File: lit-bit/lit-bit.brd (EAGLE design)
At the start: 37.5 x 49.5 mm, 71 parts, among them J2 USB_MICRO_B_SMD_FEMALE, J3 ISP, U2 32U4, U3 73831, U4 ADXL345, U5 S-1335, U6 MCP7940N, U7 24FC1025, Y1 8MHz, Y2 32.768kHz, Y3 32.768kHz, Y4 16MHz

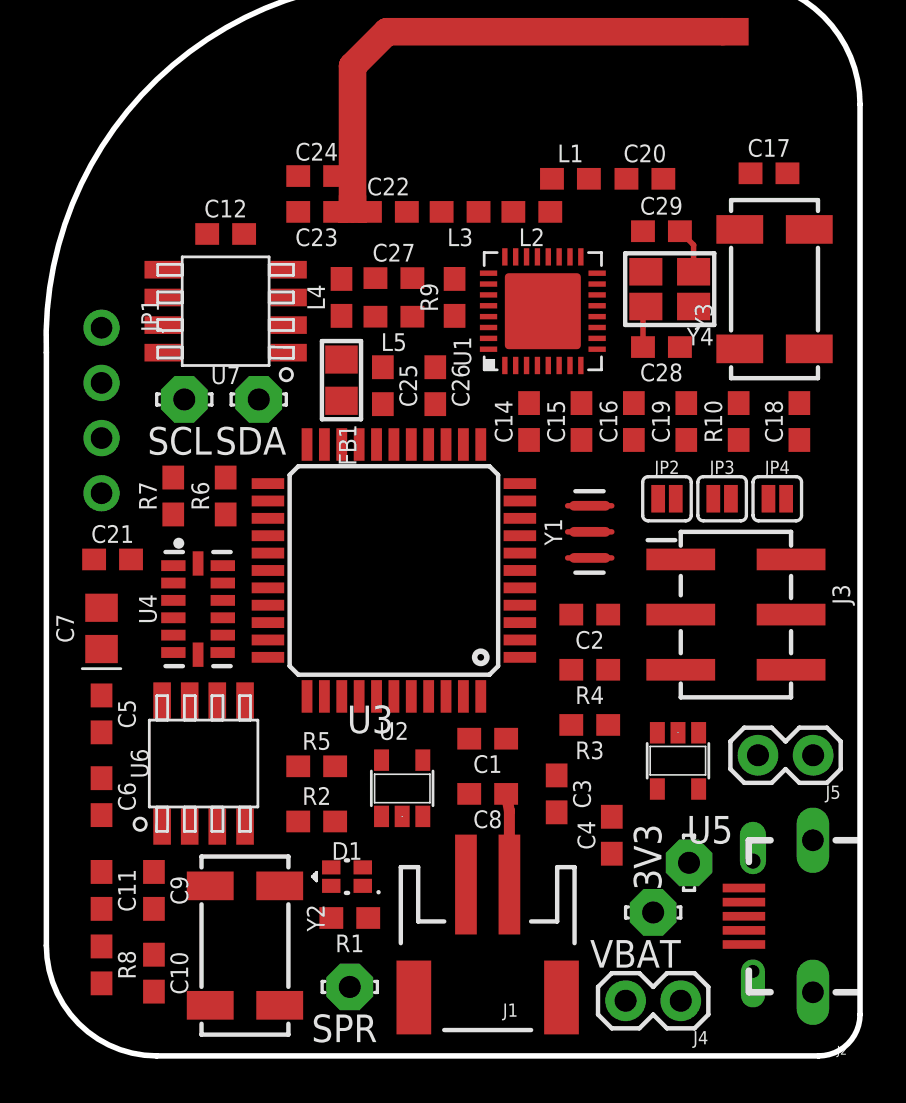
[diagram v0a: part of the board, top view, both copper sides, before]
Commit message: laid out ground planes
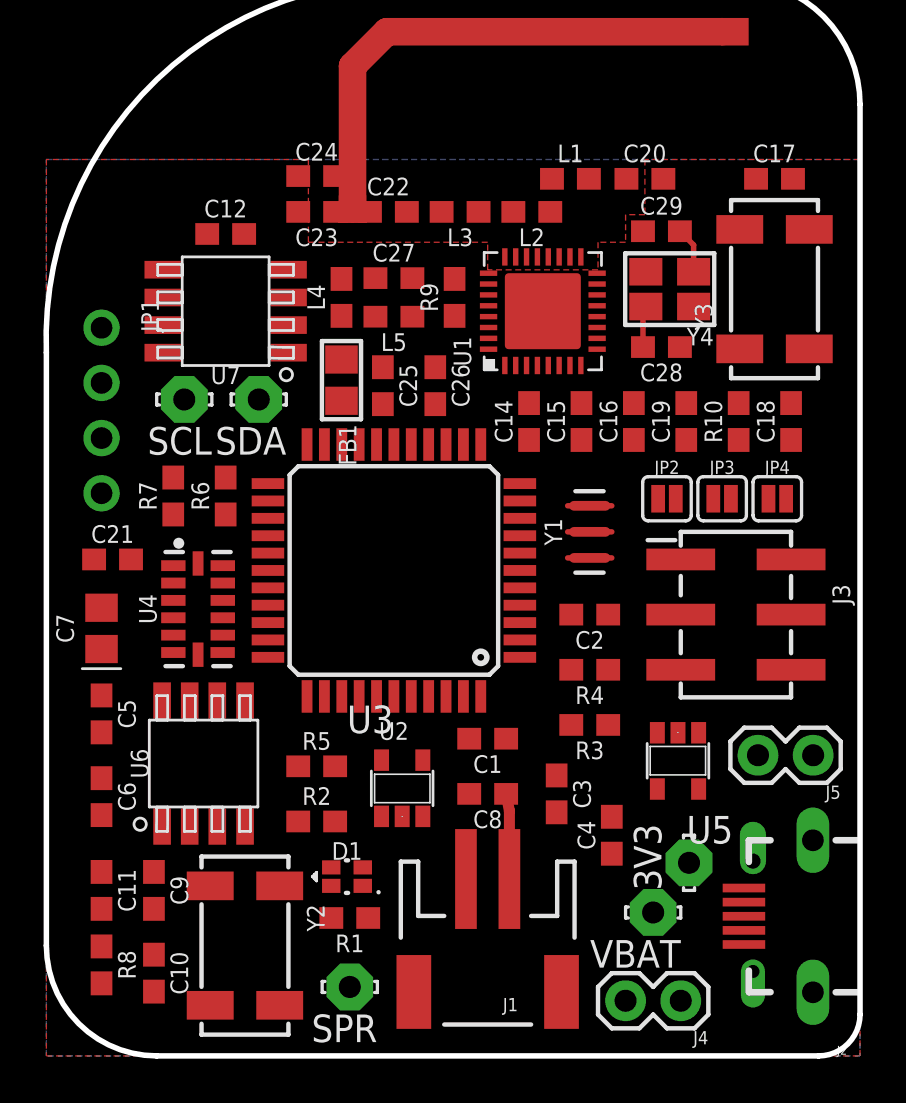
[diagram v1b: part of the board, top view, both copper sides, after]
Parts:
- moved C18 0.38 mm to (33.7, 29.2)
- moved C17 0.36 mm to (32.9, 40.4)
- moved J1 0.25 mm to (19.7, 4.45)
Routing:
- added copper zone on layer 1, net GND
- added copper zone on layer 16, net GND

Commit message: almost routed, but not working
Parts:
- R2: value 150 -> 309
- R5: value 150 -> 300
- moved Y4 16.7 mm to (11.6, 33.1), turned to 270 degrees
- moved C28 16.2 mm to (11.7, 30.2)
- moved C29 16.1 mm to (11.7, 36.1)
- moved C27 12.7 mm to (27.9, 34.2)
- moved C26 11.7 mm to (27.9, 35.7), turned to 0 degrees
- moved C6 7.62 mm to (1.91, 4.32)
- moved R8 7.62 mm to (1.91, 11.8)
- moved R10 5.64 mm to (25.7, 28.4), turned to 270 degrees
- moved C12 5.55 mm to (2.16, 36.8), turned to 90 degrees
- moved L4 5.11 mm to (17.1, 32.0), turned to 180 degrees
- moved L5 4.09 mm to (17.1, 30.4)
- moved C25 3.61 mm to (17.1, 33.7), turned to 0 degrees
- moved C19 3.54 mm to (27.9, 32.6), turned to 180 degrees
- moved C17 2.54 mm to (32.9, 37.8)
- moved Y3 2.54 mm to (32.9, 32.8)
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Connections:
- net D- renamed UD-
- net N$41 renamed VBAT-JMP
- removed net +3V3: 3V3.MP, C11.2, C12.2, C14.2, C19.2, C2.2, C21.2, C4.1, C5.2, C6.1, C7.1, J5.2, JP1.3, R6.1, R7.1, R8.2, U1.1, U1.9, U2.14, U2.24, U2.33, U2.34, U2.44, U2.6, U4.1, U4.6, U4.7, U5.5, U6.3, U6.8, U7.3, U7.8
- new net ITSYPWR: C2.2, J5.2, U2.14, U2.24, U2.33, U2.34, U2.44, U2.6
- new net UD+: J2.D+1, R4.1
- net 3V3: now also 3V3.MP, C11.2, C12.2, C14.2, C19.2, C21.2, C4.1, C5.2, C6.1, C7.1, JP1.3, R6.1, R7.1, R8.2, U1.1, U1.9, U4.1, U4.6, U4.7, U5.5, U6.8, U7.3, U7.8
- net D+: no longer J2.D+1, R4.1
- net GND: now also U6.3
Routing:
- net 3V3: track 0.00 -> 94.8 mm, vias 0 -> 8
- net ITSYPWR: track 0.00 -> 43.1 mm, vias 0 -> 2
- net SDA: track 0.00 -> 39.2 mm, vias 0 -> 4
- net AVDD: track 0.00 -> 31.5 mm, vias 0 -> 3
- net SCL: track 0.00 -> 28.8 mm, vias 0 -> 3
- net N$15: track 0.00 -> 23.0 mm
- net VBAT-JMP: track 0.00 -> 19.5 mm, vias 0 -> 1
- net VBAT: track 3.93 -> 21.1 mm
- net UD+: track 0.00 -> 16.2 mm, vias 0 -> 2
- net UD-: track 0.00 -> 14.8 mm, vias 0 -> 2
- net ACTIVE: track 0.00 -> 13.8 mm, vias 0 -> 3
- net N$21: track 0.00 -> 13.5 mm
- net N$29: track 0.00 -> 13.0 mm, vias 0 -> 2
- net N$23: track 0.00 -> 12.5 mm, vias 0 -> 2
- net MOSI: track 0.00 -> 11.6 mm, vias 0 -> 2
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
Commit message: reworking
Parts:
- moved C26 43.6 mm to (69.8, 47.8)
- moved C17 43.4 mm to (74.8, 49.3)
- moved C20 43.4 mm to (68.8, 51.8)
- moved C22 43.4 mm to (57.0, 50.3)
- moved L2 43.4 mm to (63.6, 50.3)
- moved L3 43.4 mm to (60.3, 50.3)
- moved U1 43.4 mm to (64.1, 45.7)
- moved C18 43.4 mm to (74.8, 39.1)
- moved C19 43.4 mm to (69.8, 44.1)
- moved C23 43.4 mm to (53.7, 50.3)
- moved C24 43.4 mm to (53.7, 51.9)
- moved L1 43.4 mm to (65.4, 51.8)
- moved U$28 43.4 mm to (55.4, 50.4)
- moved Y3 43.4 mm to (74.8, 44.2)
- moved C16 41.6 mm to (64.1, 39.9)
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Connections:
- net ACTIVE: no longer R10.1
- net RDYN: now also R10.1
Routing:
- net 3V3: track 94.8 -> 0.00 mm, vias 8 -> 0
- net ITSYPWR: track 43.1 -> 0.00 mm, vias 2 -> 0
- net SDA: track 39.2 -> 0.00 mm, vias 4 -> 0
- net AVDD: track 31.5 -> 0.00 mm, vias 3 -> 0
- net SCL: track 28.8 -> 0.00 mm, vias 3 -> 0
- net N$15: track 23.0 -> 0.00 mm
- net VBAT: track 21.1 -> 0.00 mm
- net VBAT-JMP: track 19.5 -> 0.00 mm, vias 1 -> 0
- net UD+: track 16.2 -> 0.00 mm, vias 2 -> 0
- net UD-: track 14.8 -> 0.00 mm, vias 2 -> 0
- net ACTIVE: track 13.8 -> 0.00 mm, vias 3 -> 0
- net N$21: track 13.5 -> 0.00 mm
- net N$29: track 13.0 -> 0.00 mm, vias 2 -> 0
- net N$23: track 12.5 -> 0.00 mm, vias 2 -> 0
- net MOSI: track 11.6 -> 0.00 mm, vias 2 -> 0
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- removed copper zone on layer 1, net GND
- removed copper zone on layer 16, net GND

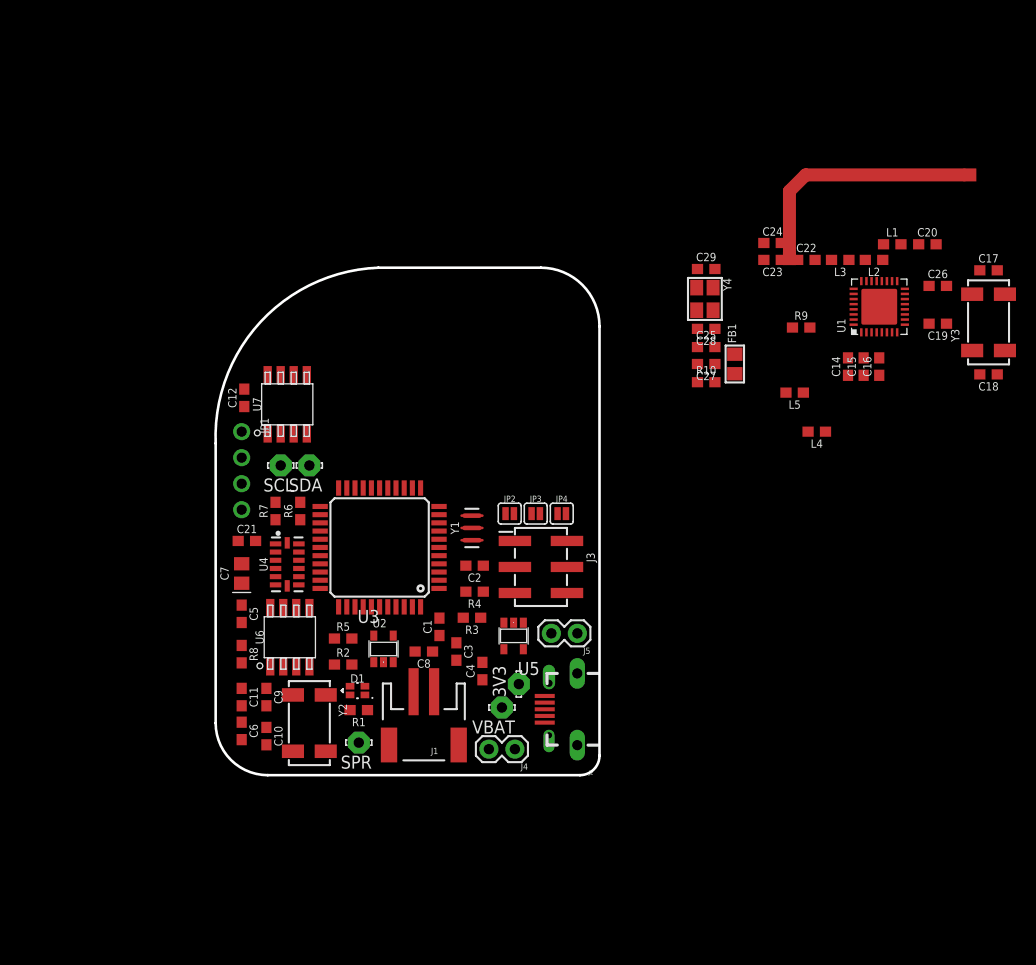
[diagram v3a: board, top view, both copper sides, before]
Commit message: routed the bluetooth module successfully
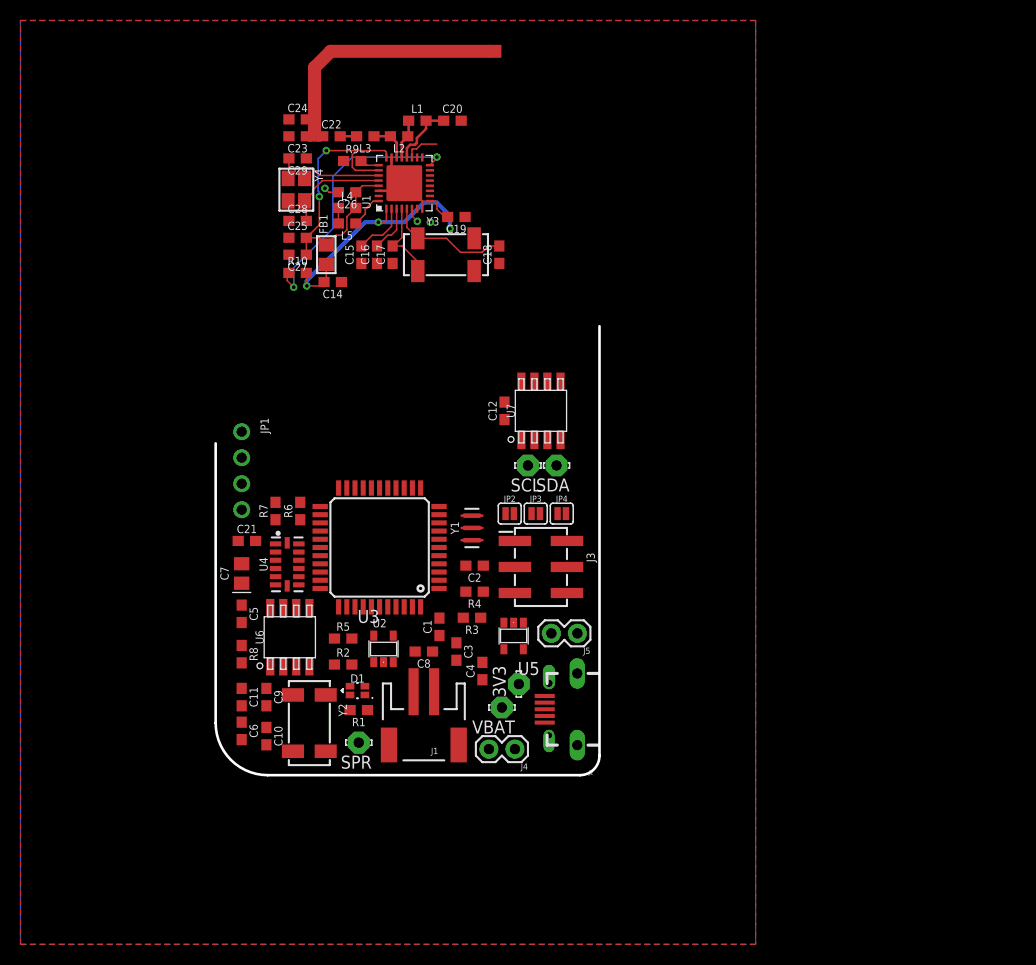
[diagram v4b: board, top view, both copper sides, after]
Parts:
- moved C26 58.4 mm to (12.2, 56.9), turned to 180 degrees
- moved C17 58.2 mm to (16.6, 50.8), turned to 90 degrees
- moved Y3 53.4 mm to (21.8, 50.8), turned to 0 degrees
- moved C14 51.0 mm to (10.8, 48.1), turned to 180 degrees
- moved L4 50.8 mm to (12.2, 55.4), turned to 0 degrees
- moved C16 50.2 mm to (15.1, 50.8)
- moved C15 50.2 mm to (13.6, 50.8)
- moved C18 49.2 mm to (27.1, 50.8), turned to 90 degrees
- moved C19 48.1 mm to (22.9, 54.5)
- moved C20 47.9 mm to (22.5, 63.9)
- moved C22 47.9 mm to (10.7, 62.4)
- moved L1 47.9 mm to (19.1, 63.9)
- moved L2 47.9 mm to (17.3, 62.4)
- moved L3 47.9 mm to (14.0, 62.4)
- moved U$28 47.9 mm to (9.02, 62.5)
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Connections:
- removed net N$26: J3.2
- net 3V3: now also J3.2
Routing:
- net AVDD: track 0.00 -> 33.4 mm, vias 0 -> 2
- net 3V3: track 0.00 -> 30.4 mm, vias 0 -> 3
- net RDYN: track 0.00 -> 26.1 mm, vias 0 -> 2
- net N$23: track 0.00 -> 12.1 mm
- net N$37: track 0.00 -> 11.7 mm
- net GND: track 0.00 -> 10.7 mm, vias 0 -> 2
- net N$33: track 0.00 -> 10.2 mm
- net N$15: track 0.00 -> 8.07 mm
- net N$24: track 0.00 -> 6.37 mm
- net N$16: track 0.00 -> 5.45 mm
- net N$22: track 0.00 -> 4.63 mm
- net N$32: track 0.00 -> 4.39 mm
- net N$28: track 0.00 -> 3.93 mm
- net N$25: track 0.00 -> 3.87 mm
- net NRF-RST: track 0.00 -> 3.43 mm
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- added copper zone on layer 1, net GND
- added copper zone on layer 16, net GND
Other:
- board size 37.5 x 49.5 mm -> 37.5 x 43.8 mm

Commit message: fukky routed, but is ugly
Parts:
- J3: device SCADA_CUSTOM_LIBRARY:2X3_SMD_HAND_SOLDER -> SCADA_CUSTOM_LIBRARY:2X3
- moved C18 37.0 mm to (39.9, 16.1), turned to 180 degrees
- moved C15 36.4 mm to (31.6, 19.2)
- moved C16 36.4 mm to (33.1, 19.2)
- moved C17 36.4 mm to (34.7, 19.2)
- moved C19 36.4 mm to (40.9, 22.9)
- moved C20 36.4 mm to (40.5, 32.3)
- moved C22 36.4 mm to (28.7, 30.7)
- moved C23 36.4 mm to (25.4, 30.7)
- moved C24 36.4 mm to (25.4, 32.4)
- moved C25 36.4 mm to (25.4, 20.8)
- moved C26 36.4 mm to (30.2, 25.3)
- moved C27 36.4 mm to (25.4, 19.2)
- moved C28 36.4 mm to (25.4, 22.5)
- moved C29 36.4 mm to (25.4, 28.6)
- moved FB1 36.4 mm to (28.2, 19.2)
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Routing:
- net 3V3: track 30.4 -> 110.1 mm, vias 3 -> 4
- net MOSI: track 0.00 -> 74.8 mm, vias 0 -> 6
- net SCK: track 0.00 -> 73.6 mm, vias 0 -> 6
- net NRF-RST: track 3.43 -> 52.5 mm, vias 0 -> 4
- net SCL: track 0.00 -> 46.8 mm, vias 0 -> 4
- net ITSYPWR: track 0.00 -> 45.7 mm
- net SDA: track 0.00 -> 43.0 mm, vias 0 -> 5
- net REQN: track 0.00 -> 41.2 mm, vias 0 -> 2
- net MISO: track 0.00 -> 40.1 mm, vias 0 -> 4
- net VUSB: track 0.00 -> 34.0 mm, vias 0 -> 5
- net ACTIVE: track 1.44 -> 33.4 mm, vias 1 -> 5
- net RTC-INT: track 0.00 -> 26.0 mm, vias 0 -> 2
- net VBAT: track 0.00 -> 25.4 mm
- net D+: track 0.00 -> 24.8 mm, vias 0 -> 4
- net N$6: track 0.00 -> 21.8 mm, vias 0 -> 4
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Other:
- board outline removed

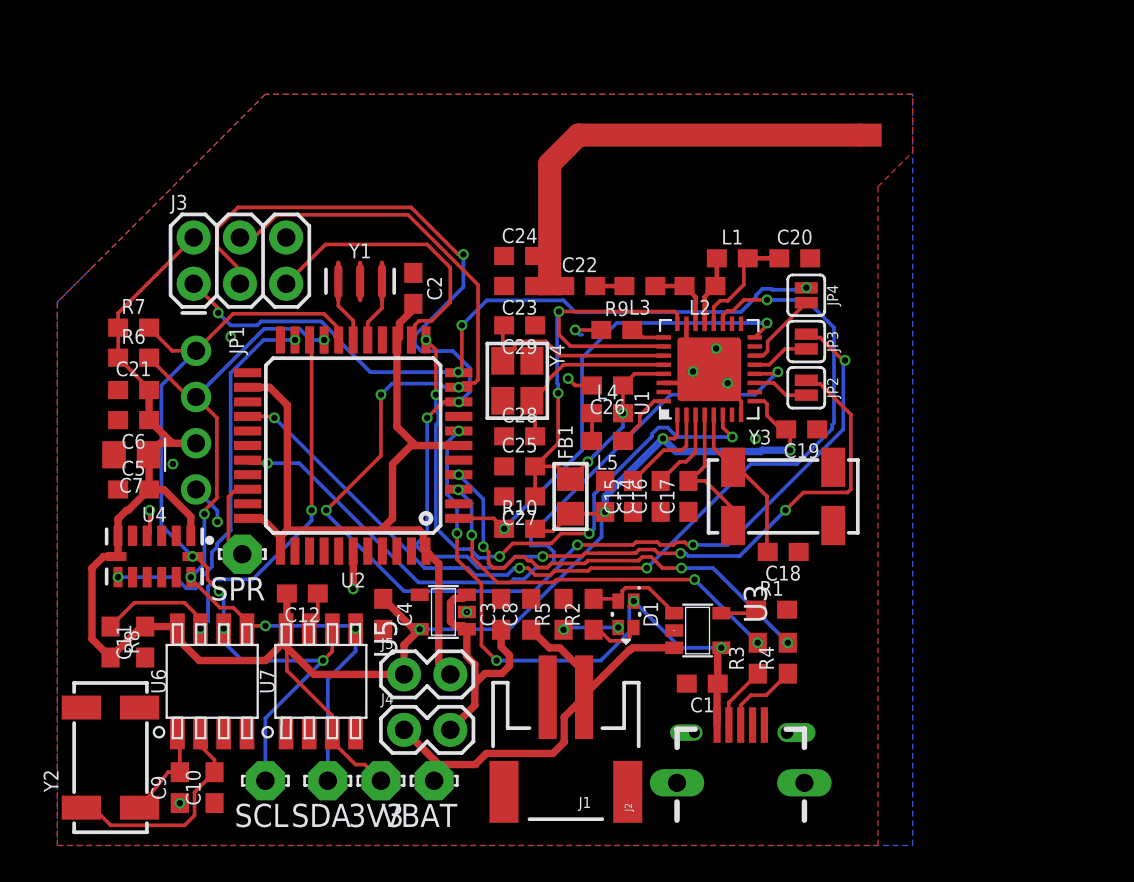
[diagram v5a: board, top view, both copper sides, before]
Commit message: rotated the nrf module, having better luck but is still bad
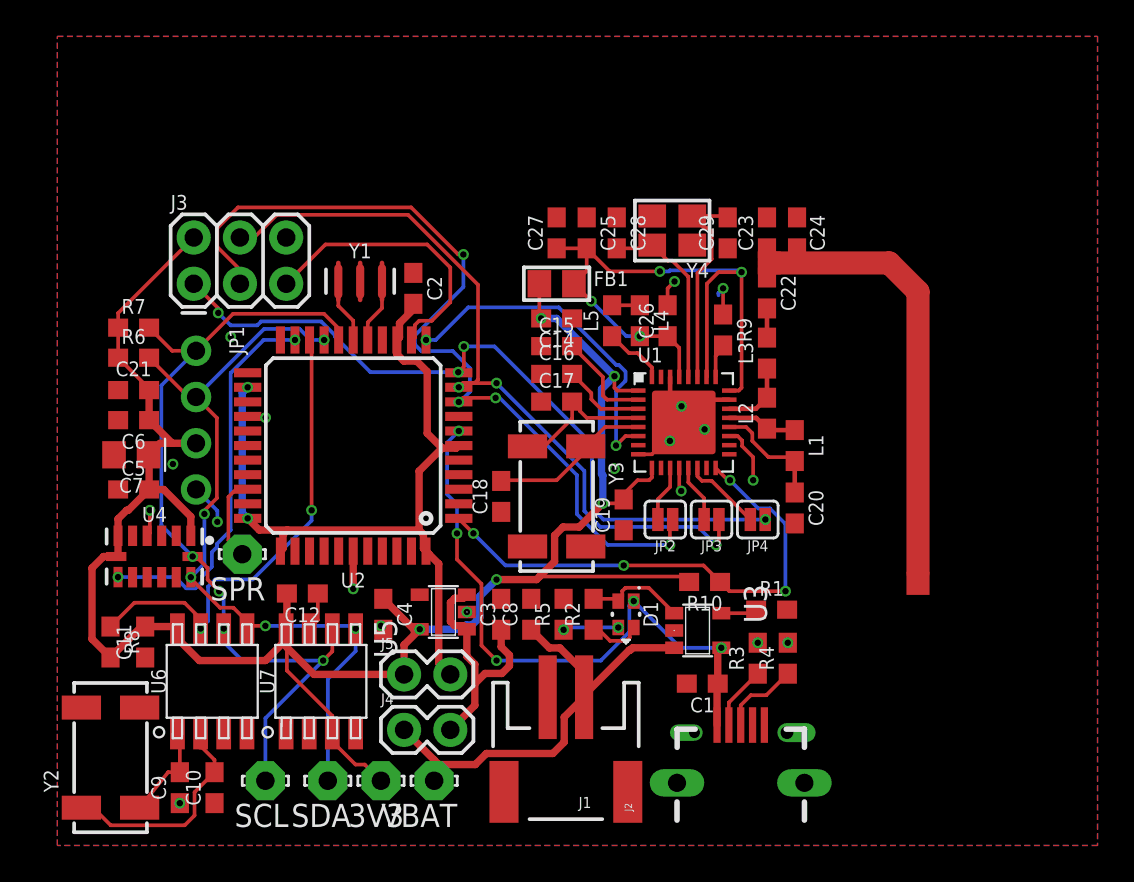
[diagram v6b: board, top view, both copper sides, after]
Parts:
- moved C18 15.8 mm to (24.4, 19.2), turned to 90 degrees
- moved C24 15.3 mm to (40.6, 33.7), turned to 90 degrees
- moved C27 14.6 mm to (27.4, 33.7), turned to 90 degrees
- moved C23 13.9 mm to (39.0, 33.7), turned to 90 degrees
- moved C20 13.7 mm to (40.5, 18.5), turned to 270 degrees
- moved C25 13.3 mm to (29.1, 33.7), turned to 270 degrees
- moved JP4 12.6 mm to (38.5, 17.9), turned to 180 degrees
- moved C29 12.5 mm to (36.8, 33.7), turned to 90 degrees
- moved Y3 12.4 mm to (27.4, 19.2), turned to 270 degrees
- moved C28 12.4 mm to (30.7, 33.7), turned to 270 degrees
- moved U$28 12.1 mm to (39.1, 32.0), turned to 180 degrees
- moved Y4 11.9 mm to (33.8, 33.8), turned to 180 degrees
- moved FB1 11.7 mm to (27.4, 30.9), turned to 0 degrees
- moved JP3 11.1 mm to (35.9, 17.9), turned to 180 degrees
- moved C19 10.8 mm to (31.1, 18.2), turned to 90 degrees
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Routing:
- net NRF-RST: track 52.5 -> 4.25 mm, vias 4 -> 2
- net REQN: track 41.2 -> 1.31 mm, vias 2 -> 1
- net MOSI: track 74.8 -> 42.6 mm, vias 6 -> 3
- net SCK: track 73.6 -> 48.4 mm, vias 6 -> 4
- net D+: track 24.8 -> 0.00 mm, vias 4 -> 1
- net N$6: track 21.8 -> 0.00 mm, vias 4 -> 1
- net ACTIVE: track 33.4 -> 18.9 mm, vias 5 -> 2
- net 3V3: track 110.1 -> 116.9 mm, vias 4 -> 5
- net ITSYPWR: track 45.7 -> 43.1 mm, vias 0 -> 2
- net RDYN: track 25.9 -> 28.4 mm, vias 2 -> 4
- net MISO: track 40.1 -> 41.1 mm
- net GND: vias 13 -> 14

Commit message: finally have something decent
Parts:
- moved R10 3.86 mm to (39.4, 15.1)
- moved J2 1.42 mm to (41.9, 0.00)
- moved Y4 0.90 mm to (34.4, 34.4)
- moved L1 0.90 mm to (41.1, 22.6)
- moved L2 0.90 mm to (39.6, 24.4)
- moved L3 0.90 mm to (39.6, 27.7)
- moved R4 0.90 mm to (40.8, 9.65)
- moved C14 0.90 mm to (28.1, 29.6)
- moved C15 0.90 mm to (28.1, 28.1)
- moved Y3 0.90 mm to (28.1, 19.8)
- moved C20 0.90 mm to (41.1, 19.2)
- moved C22 0.90 mm to (39.6, 31.0)
- moved C23 0.90 mm to (39.6, 34.3)
- moved C29 0.90 mm to (37.5, 34.3)
- moved L4 0.90 mm to (32.6, 29.5)
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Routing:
- net NRF-RST: track 4.25 -> 41.2 mm, vias 2 -> 6
- net D+: track 0.00 -> 27.1 mm, vias 1 -> 3
- net REQN: track 1.31 -> 28.3 mm, vias 1 -> 4
- net N$6: track 0.00 -> 21.5 mm, vias 1 -> 3
- net GND: track 20.6 -> 25.5 mm, vias 14 -> 18
- net 3V3: track 116.9 -> 121.3 mm
- net RDYN: track 28.4 -> 27.3 mm
- net SCK: track 48.4 -> 47.5 mm, vias 4 -> 3
- net MISO: track 41.1 -> 40.2 mm
- net MOSI: track 42.6 -> 41.7 mm, vias 3 -> 2
- net VUSB: track 34.0 -> 34.8 mm
- net UD+: track 4.39 -> 5.03 mm
- net UD-: track 3.48 -> 4.11 mm
- net N$21: track 12.1 -> 12.7 mm
- net ACTIVE: track 18.9 -> 19.5 mm
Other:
- board outline added: 50.2 x 36.8 mm

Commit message: added gnd point for testing
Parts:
- added GND: (no value), microbuilder:1X01_ROUND
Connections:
- net GND: now also GND.1
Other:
- board text added: "Designed by: Alexander "Smitty" Smith"
